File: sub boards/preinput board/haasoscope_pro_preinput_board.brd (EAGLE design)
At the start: 94.2 x 41.9 mm, 31 parts, among them J4 8pin, K1 G6K-2F-RF-T-TR03_DC5, K2 G6K-2F-RF-T-TR03_DC5, K3 TLP3475R_TP,F, K5 G6K-2F-RF-T-TR03_DC5, Q1 S8050, Q2 S8050, Q3 S8050

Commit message: Deemphasis filter
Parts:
- added C3: RF_1pF, MF_Passives:C0402
- added R14: 12, MF_Passives:R0402
- added R4, R5: 357, MF_Passives:R0402
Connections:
- new net BNCIN1: BNCIN.SIGNAL, C3.P$1, R14.P$2, R4.P$2
- net GND: now also R4.P$1, R5.P$1
- net INPATH: now also C3.P$2, R14.P$1, R5.P$2; no longer BNCIN.SIGNAL
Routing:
- net BNCIN1: track 0.00 -> 11.2 mm
- net INPATH: track 15.7 -> 10.9 mm
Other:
- board text added: "Haasoscope Pro Pre-input board, v1.40 Cutouts, demphasis filter by Dr. Andy Haas November 2024"
- board text removed: "Haasoscope Pro Pre-input board, v1.31, cutouts by Dr. Andy Haas October 2024"
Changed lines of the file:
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@@
 <wire x1="85" y1="8.1" x2="85" y2="50" width="0.254" layer="20"/>
 <wire x1="85" y1="50" x2="-9.2" y2="50" width="0.254" layer="20"/>
-<text x="56.6" y="42.9" size="0.8128" layer="21">Haasoscope Pro
-Pre-input board, v1.31, cutouts
+<text x="60.7" y="42.3" size="0.8128" layer="21">Haasoscope Pro
+Pre-input board, v1.40
+Cutouts, demphasis filter
 by Dr. Andy Haas
-October 2024</text>
+November 2024</text>
 <text x="33.3" y="45.4" size="0.8128" layer="21" rot="R270">GND</text>
 <text x="38.4" y="45.4" size="0.8128" layer="21" rot="R270">AC/DC</text>
@@
 <attribute name="DIGIKEY" value="WM5524-ND" x="28.4" y="45.8" size="1.778" layer="27" rot="R270" display="off"/>
 <attribute name="MPN" value="73100-0105" x="28.4" y="45.8" size="1.778" layer="27" rot="R270" display="off"/>
-<attribute name="NAME" x="0.5" y="31.3" size="0.8128" layer="25" font="vector" rot="R270" align="bottom-center"/>
+<attribute name="NAME" x="0.5" y="31.3" size="0.8128" layer="21" font="vector" rot="R270" align="bottom-center"/>
 </element>
 <element name="Q1" library="Seeed-Transistor" library_urn="urn:adsk.eagle:library:477" package="SOT-23" package3d_urn="urn:adsk.eagle:package:33015/1" value="S8050" x="35.7" y="38.4" smashed="yes" rot="R270">
@@
 <attribute name="MOUSER_PART_NUMBER" value="653-G6K2FRFTTR03DC5" x="65.1" y="42.8" size="0.8128" layer="27" rot="R270" display="off"/>
 <attribute name="MOUSER_PRICE-STOCK" value="https://www.mouser.co.uk/ProductDetail/Omron-Electronics/G6K-2F-RF-T-TR03-DC5?qs=bR9%2Fh8%2FHa7Q3LGohyKHVjA%3D%3D" x="65.1" y="42.8" size="0.8128" layer="27" rot="R270" display="off"/>
+</element>
+<element name="R4" library="MF_Passives" package="R0402" value="357" x="3.3" y="23.2" smashed="yes" rot="R90">
+<attribute name="HOUSEPART" value="" x="3.3" y="23.2" size="1.778" layer="27" rot="R90" display="off"/>
+<attribute name="MPN" value="" x="3.3" y="23.2" size="1.778" layer="27" rot="R90" display="off"/>
+<attribute name="NAME" x="2.5" y="22.6" size="0.8128" layer="21" font="vector" rot="R90"/>
+<attribute name="POPULATE" value="1" x="3.3" y="23.2" size="1.778" layer="27" rot="R90" display="off"/>
+<attribute name="TOLERANCE" value="" x="3.3" y="23.2" size="1.778" layer="27" rot="R90" display="off"/>
+<attribute name="URL" value="" x="3.3" y="23.2" size="1.778" layer="27" rot="R90" display="off"/>
+<attribute name="VOLTAGE" value="" x="3.3" y="23.2" size="1.778" layer="27" rot="R90" display="off"/>
+<attribute name="WATTAGE" value="" x="3.3" y="23.2" size="1.778" layer="27" rot="R90" display="off"/>
+</element>
+<element name="R5" library="MF_Passives" package="R0402" value="357" x="4.7" y="23.2" smashed="yes" rot="R90">
+<attribute name="HOUSEPART" value="" x="4.7" y="23.2" size="1.778" layer="27" rot="R90" display="off"/>
+<attribute name="MPN" value="" x="4.7" y="23.2" size="1.778" layer="27" rot="R90" display="off"/>
+<attribute name="NAME" x="5.5" y="23.7" size="0.8128" layer="21" font="vector" rot="R270"/>
+<attribute name="POPULATE" value="1" x="4.7" y="23.2" size="1.778" layer="27" rot="R90" display="off"/>
+<attribute name="TOLERANCE" value="" x="4.7" y="23.2" size="1.778" layer="27" rot="R90" display="off"/>
+<attribute name="URL" value="" x="4.7" y="23.2" size="1.778" layer="27" rot="R90" display="off"/>
+<attribute name="VOLTAGE" value="" x="4.7" y="23.2" size="1.778" layer="27" rot="R90" display="off"/>
+<attribute name="WATTAGE" value="" x="4.7" y="23.2" size="1.778" layer="27" rot="R90" display="off"/>
+</element>
+<element name="R14" library="MF_Passives" package="R0402" value="12" x="4" y="25.1" smashed="yes" rot="R180">
+<attribute name="HOUSEPART" value="" x="4" y="25.1" size="1.778" layer="27" rot="R180" display="off"/>
+<attribute name="MPN" value="" x="4" y="25.1" size="1.778" layer="27" rot="R180" display="off"/>
+<attribute name="NAME" x="5.4" y="24.8" size="0.8128" layer="21" font="vector"/>
+<attribute name="POPULATE" value="1" x="4" y="25.1" size="1.778" layer="27" rot="R180" display="off"/>
+<attribute name="TOLERANCE" value="" x="4" y="25.1" size="1.778" layer="27" rot="R180" display="off"/>
+<attribute name="URL" value="" x="4" y="25.1" size="1.778" layer="27" rot="R180" display="off"/>
+<attribute name="VOLTAGE" value="" x="4" y="25.1" size="1.778" layer="27" rot="R180" display="off"/>
+<attribute name="WATTAGE" value="" x="4" y="25.1" size="1.778" layer="27" rot="R180" display="off"/>
+</element>
+<element name="C3" library="MF_Passives" package="C0402" value="RF_1pF" x="4" y="26.4" smashed="yes">
+<attribute name="DIELECTRIC" value="" x="4" y="26.4" size="1.778" layer="27" display="off"/>
+<attribute name="HOUSEPART" value="" x="4" y="26.4" size="1.778" layer="27" display="off"/>
+<attribute name="LCSC" value="C52923" x="4" y="26.4" size="1.778" layer="27" display="off"/>
+<attribute name="MPN" value="" x="4" y="26.4" size="1.778" layer="27" display="off"/>
+<attribute name="NAME" x="5.4" y="26.1" size="0.8128" layer="21" font="vector"/>
+<attribute name="POPULATE" value="1" x="4" y="26.4" size="1.778" layer="27" display="off"/>
+<attribute name="TOLERANCE" value="" x="4" y="26.4" size="1.778" layer="27" display="off"/>
+<attribute name="URL" value="" x="4" y="26.4" size="1.778" layer="27" display="off"/>
+<attribute name="VOLTAGE" value="" x="4" y="26.4" size="1.778" layer="27" display="off"/>
 </element>
 </elements>
@@
 <via x="59.1" y="26.7" extent="1-16" drill="0.35"/>
 <via x="59.2" y="24" extent="1-16" drill="0.35"/>
-<via x="8.7" y="27.9" extent="1-16" drill="0.35"/>
-<via x="8.1" y="24.2" extent="1-16" drill="0.35"/>
-<via x="3.5" y="28.2" extent="1-16" drill="0.35"/>
-<via x="5.2" y="32.1" extent="1-16" drill="0.35"/>
-<via x="3.3" y="38.7" extent="1-16" drill="0.35"/>
+<via x="8" y="26.5" extent="1-16" drill="0.35"/>
+<via x="8" y="23.8" extent="1-16" drill="0.35"/>
+<via x="0.7" y="24.4" extent="1-16" drill="0.35"/>
+<via x="4.6" y="33.1" extent="1-16" drill="0.35"/>
+<via x="4.6" y="36.6" extent="1-16" drill="0.35"/>
 <via x="15.7" y="29.4" extent="1-16" drill="0.35"/>
 <via x="33.7" y="29.4" extent="1-16" drill="0.35"/>
@@
 <vertex x="46.07" y="20.77"/>
 </polygon>
+<contactref element="R4" pad="P$1"/>
+<contactref element="R5" pad="P$1"/>
+<via x="3.1" y="21.8" extent="1-16" drill="0.35"/>
+<via x="4.8" y="21.8" extent="1-16" drill="0.35"/>
+<via x="2.1" y="28.1" extent="1-16" drill="0.35"/>
+<via x="4.5" y="28.2" extent="1-16" drill="0.35"/>
 </signal>
 <signal name="VS+" airwireshidden="yes">
@@
 </signal>
 <signal name="INPATH">
-<contactref element="BNCIN" pad="SIGNAL"/>
 <contactref element="K1" pad="3"/>
+<contactref element="R5" pad="P$2"/>
+<contactref element="R14" pad="P$1"/>
+<contactref element="C3" pad="P$2"/>
+<wire x1="4.55" y1="26.4" x2="4.55" y2="25.1" width="0.254" layer="1"/>
+<wire x1="4.6294" y1="25.0206" x2="4.55" y2="25.1" width="0.254" layer="1"/>
 <wire x1="12.7" y1="25" x2="12.6794" y2="25.0206" width="0.254" layer="1"/>
-<wire x1="12.6794" y1="25.0206" x2="9.18426875" y2="25.0206" width="0.254" layer="1"/>
-<wire x1="9.18426875" y1="25.0206" x2="3.3" y2="30.90486875" width="0.254" layer="1"/>
-<wire x1="3.3" y1="30.90486875" x2="3.3" y2="34.8" width="0.254" layer="1"/>
+<wire x1="12.6794" y1="25.0206" x2="4.6294" y2="25.0206" width="0.254" layer="1"/>
+<wire x1="4.7" y1="23.75" x2="4.7" y2="24.95" width="0.254" layer="1"/>
+<wire x1="4.7" y1="24.95" x2="4.55" y2="25.1" width="0.254" layer="1"/>
 </signal>
 <signal name="ACDC_CONTROL">
@@
 <wire x1="48.5" y1="27.3" x2="54.5" y2="27.3" width="0.6096" layer="1"/>
 </signal>
+<signal name="BNCIN1">
+<contactref element="BNCIN" pad="SIGNAL"/>
+<contactref element="R4" pad="P$2"/>
+<contactref element="R14" pad="P$2"/>
+<contactref element="C3" pad="P$1"/>
+<wire x1="3.3" y1="34.8" x2="3.3" y2="26.55" width="0.254" layer="1"/>
+<wire x1="3.3" y1="26.55" x2="3.45" y2="26.4" width="0.254" layer="1"/>
+<wire x1="3.45" y1="26.4" x2="3.45" y2="25.1" width="0.254" layer="1"/>
+<wire x1="3.45" y1="25.1" x2="3.45" y2="23.9" width="0.254" layer="1"/>
+<wire x1="3.45" y1="23.9" x2="3.3" y2="23.75" width="0.254" layer="1"/>
+</signal>
 </signals>

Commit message: 27 pF
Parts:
- C3: value RF_1pF -> RF_27pF
- R14: value 12 -> 15
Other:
- board text added: "Haasoscope Pro Pre-input board, v1.40 Cutouts, de-emphasis filter by Dr. Andy Haas November 2024"
- board text removed: "Haasoscope Pro Pre-input board, v1.40 Cutouts, demphasis filter by Dr. Andy Haas November 2024"
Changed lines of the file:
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@@
 <text x="60.7" y="42.3" size="0.8128" layer="21">Haasoscope Pro
 Pre-input board, v1.40
-Cutouts, demphasis filter
+Cutouts, de-emphasis filter
 by Dr. Andy Haas
 November 2024</text>
@@
 <attribute name="WATTAGE" value="" x="4.7" y="23.2" size="1.778" layer="27" rot="R90" display="off"/>
 </element>
-<element name="R14" library="MF_Passives" package="R0402" value="12" x="4" y="25.1" smashed="yes" rot="R180">
+<element name="R14" library="MF_Passives" package="R0402" value="15" x="4" y="25.1" smashed="yes" rot="R180">
 <attribute name="HOUSEPART" value="" x="4" y="25.1" size="1.778" layer="27" rot="R180" display="off"/>
 <attribute name="MPN" value="" x="4" y="25.1" size="1.778" layer="27" rot="R180" display="off"/>
@@
 <attribute name="WATTAGE" value="" x="4" y="25.1" size="1.778" layer="27" rot="R180" display="off"/>
 </element>
-<element name="C3" library="MF_Passives" package="C0402" value="RF_1pF" x="4" y="26.4" smashed="yes">
+<element name="C3" library="MF_Passives" package="C0402" value="RF_27pF" x="4" y="26.4" smashed="yes">
 <attribute name="DIELECTRIC" value="" x="4" y="26.4" size="1.778" layer="27" display="off"/>
 <attribute name="HOUSEPART" value="" x="4" y="26.4" size="1.778" layer="27" display="off"/>

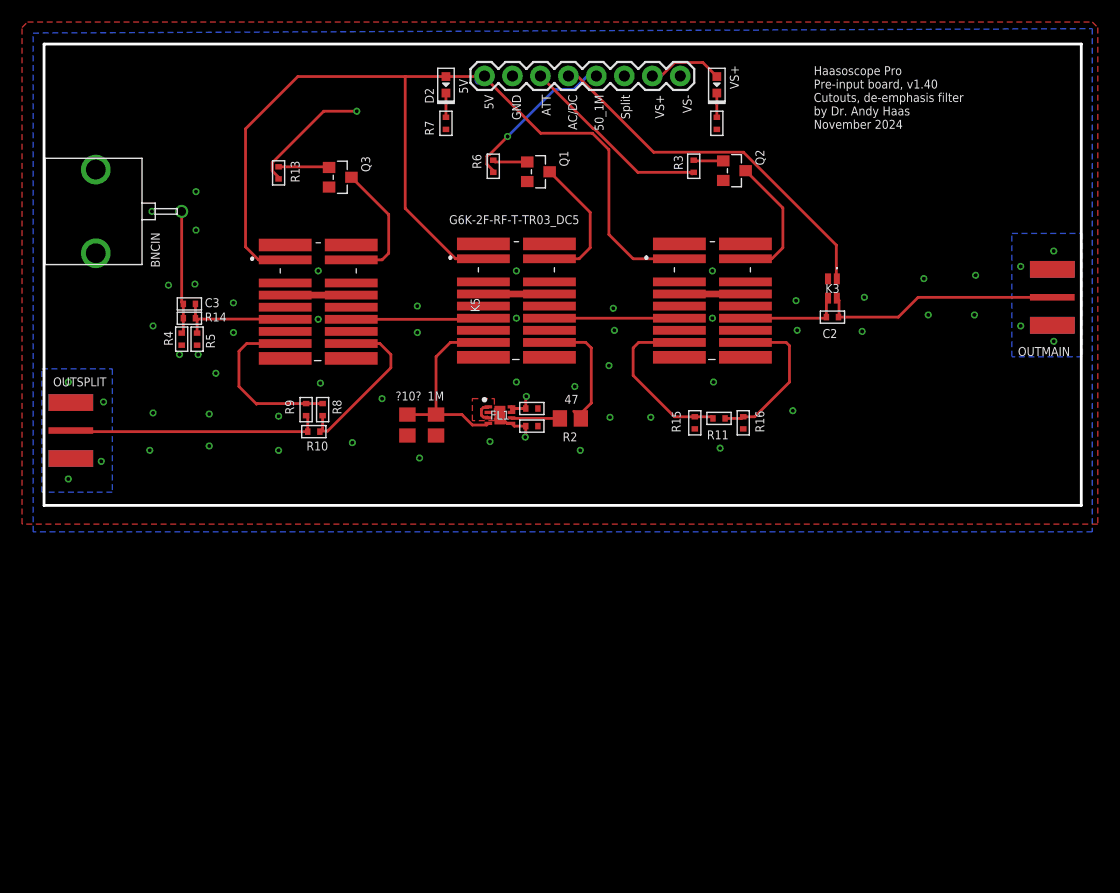
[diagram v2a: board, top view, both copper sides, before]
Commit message: try low pass 1.25 and 2.5 GHz filters
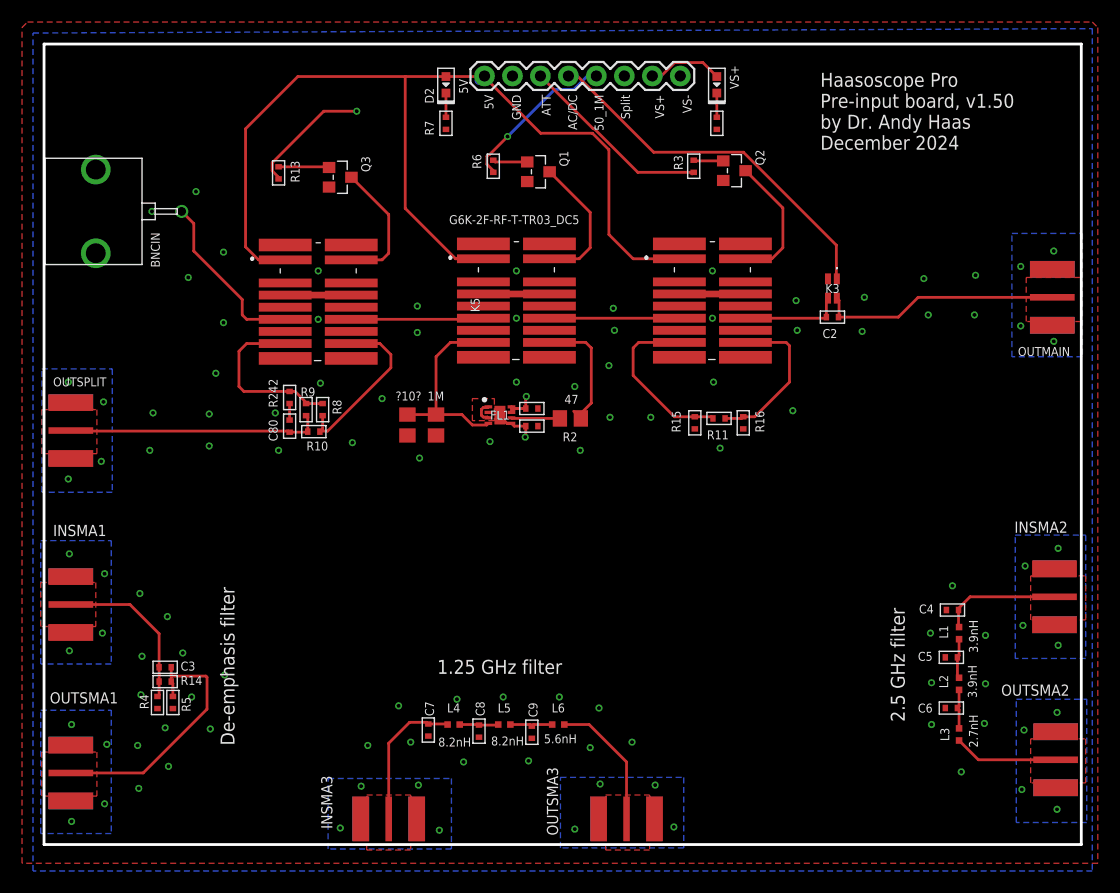
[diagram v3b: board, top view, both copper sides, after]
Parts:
- added C4: 2pF, MF_Passives:C0402
- added C5, C6: 3pF, MF_Passives:C0402
- added C7: 4.3pF, MF_Passives:C0402
- added C8, C9: 6.2pF, MF_Passives:C0402
- added C80: 27pF, MF_Passives:C0402
- added INSMA1, INSMA2, INSMA3, OUTSMA1, OUTSMA2, OUTSMA3: out50, adafruit:SMA_EDGELAUNCH
- added L1, L2: 3.9nH, Nordic_nRF:RESC0402_N
- added L3: 2.7nH, Nordic_nRF:RESC0402_N
- added L4, L5: 8.2nH, Nordic_nRF:RESC0402_N
- added L6: 5.6nH, Nordic_nRF:RESC0402_N
- added R242: 27, MF_Passives:R0402
- moved C3 33.1 mm to (1.80, -6.60)
- moved R14 33.1 mm to (1.80, -7.90)
- moved R4 33.1 mm to (1.10, -9.80)
- moved R5 33.1 mm to (2.50, -9.80)
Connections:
- removed net BNCIN1: BNCIN.SIGNAL, C3.P$1, R14.P$2, R4.P$2
- new net N$10: C8.P$1, L4.2, L5.1
- new net N$11: C9.P$1, L5.2, L6.1
- new net N$67: C80.P$1, R242.P$2
- new net N$8: C5.P$1, L1.2, L2.1
- new net N$9: C6.P$1, L2.2, L3.1
- new net SMAIN1: C3.P$1, INSMA1.P, R14.P$2, R4.P$2
- new net SMAIN2: C4.P$1, INSMA2.P, L1.1
- new net SMAIN3: C7.P$1, INSMA3.P, L4.1
- new net SMAOUT1: C3.P$2, OUTSMA1.P, R14.P$1, R5.P$2
- new net SMAOUT2: L3.2, OUTSMA2.P
- new net SMAOUT3: L6.2, OUTSMA3.P
- net GND: now also C4.P$2, C5.P$2, C6.P$2, C7.P$2, C8.P$2, C9.P$2, INSMA1.GND@1, INSMA1.GND@2, INSMA1.GND@3, INSMA1.GND@4, INSMA2.GND@1, INSMA2.GND@2, INSMA2.GND@3, INSMA2.GND@4, INSMA3.GND@1, INSMA3.GND@2, INSMA3.GND@3, INSMA3.GND@4, OUTSMA1.GND@1, OUTSMA1.GND@2, OUTSMA1.GND@3, OUTSMA1.GND@4, OUTSMA2.GND@1, OUTSMA2.GND@2, OUTSMA2.GND@3, OUTSMA2.GND@4, OUTSMA3.GND@1, OUTSMA3.GND@2, OUTSMA3.GND@3, OUTSMA3.GND@4
- net INPATH: now also BNCIN.SIGNAL; no longer C3.P$2, R14.P$1, R5.P$2
- net OUTSPLIT: now also C80.P$2
- net SPLIT: now also R242.P$1
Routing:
- net SMAOUT1: track 0.00 -> 23.7 mm
- net SMAIN1: track 0.00 -> 15.1 mm
- net SMAIN3: track 0.00 -> 13.1 mm
- net SMAOUT3: track 0.00 -> 12.2 mm
- net BNCIN1: track 11.2 -> 0.00 mm
- net SMAIN2: track 0.00 -> 10.9 mm
- net SMAOUT2: track 0.00 -> 9.49 mm
- net INPATH: track 10.9 -> 15.8 mm
- net N$11: track 0.00 -> 3.92 mm
- net N$9: track 0.00 -> 3.62 mm
- net N$8: track 0.00 -> 3.62 mm
- net N$10: track 0.00 -> 3.54 mm
- net N$67: track 0.00 -> 1.50 mm
- added copper zone on layer 1, net GND1
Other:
- board size 94.2 x 41.9 mm -> 94.2 x 72.7 mm
- board text added: "1.25 GHz filter"
- board text added: "2.5 GHz filter"
- board text added: "De-emphasis filter"
- board text added: "Haasoscope Pro Pre-input board, v1.50 by Dr. Andy Haas December 2024"
- board text removed: "Haasoscope Pro Pre-input board, v1.40 Cutouts, de-emphasis filter by Dr. Andy Haas November 2024"
